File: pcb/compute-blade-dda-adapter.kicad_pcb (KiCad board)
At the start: 2 copper layers, 35.5 x 28.8 mm, 2 parts, among them J1 COMPUTE BLADE, J2 DDA GPS/RTC RIGHT-ANGLE

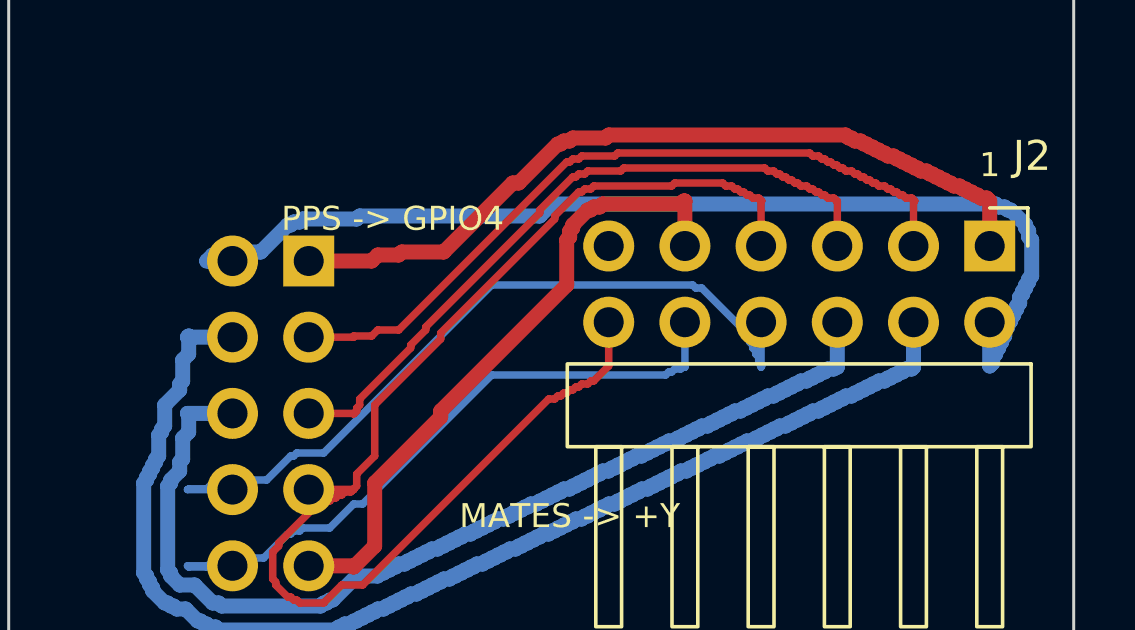
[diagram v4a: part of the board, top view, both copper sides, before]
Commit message: Preserve connector pad escapes during routing
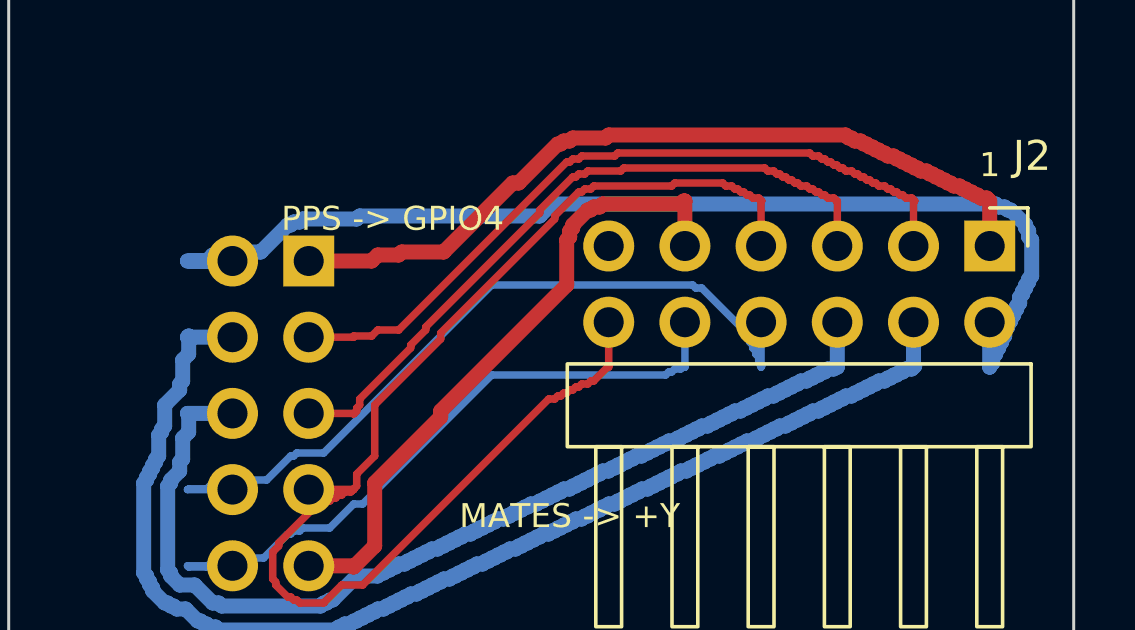
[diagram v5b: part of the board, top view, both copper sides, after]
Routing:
- net 5V_PIN2: track 36.1 -> 37.4 mm
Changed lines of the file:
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@@
   (segment (start 119.8 63.86) (end 119.9 63.76) (width 0.5) (layer "B.Cu") (net 4))
   (segment (start 119.9 63.76) (end 120.1 63.76) (width 0.5) (layer "B.Cu") (net 4))
-  (segment (start 120.1 63.76) (end 120.16 63.7) (width 0.5) (layer "B.Cu") (net 4))
+  (segment (start 120.1 63.76) (end 120.2 63.66) (width 0.5) (layer "B.Cu") (net 4))
+  (segment (start 120.2 63.66) (end 120.16 63.7) (width 0.5) (layer "B.Cu") (net 4))
   (segment (start 120.16 63.7) (end 120.16 62.2) (width 0.5) (layer "B.Cu") (net 4))
-  (segment (start 97.46 60.16) (end 96.6 60.16) (width 0.5) (layer "B.Cu") (net 2))
+  (segment (start 97.46 60.16) (end 95.96 60.16) (width 0.5) (layer "B.Cu") (net 2))
+  (segment (start 95.96 60.16) (end 96.6 60.16) (width 0.5) (layer "B.Cu") (net 2))
   (segment (start 96.6 60.16) (end 96.8 59.96) (width 0.5) (layer "B.Cu") (net 2))
   (segment (start 96.8 59.96) (end 97.5 59.96) (width 0.5) (layer "B.Cu") (net 2))
@@
   (segment (start 122.8 63.36) (end 122.8 63.56) (width 0.5) (layer "B.Cu") (net 2))
   (segment (start 122.8 63.56) (end 122.7 63.66) (width 0.5) (layer "B.Cu") (net 2))
-  (segment (start 122.7 63.66) (end 122.7 62.2) (width 0.5) (layer "B.Cu") (net 2))
-  (segment (start 110 62.2) (end 110 63.66) (width 0.25) (layer "F.Cu") (net 7))
+  (segment (start 122.7 63.66) (end 122.7 63.7) (width 0.5) (layer "B.Cu") (net 2))
+  (segment (start 122.7 63.7) (end 122.7 62.2) (width 0.5) (layer "B.Cu") (net 2))
+  (segment (start 110 62.2) (end 110 63.7) (width 0.25) (layer "F.Cu") (net 7))
+  (segment (start 110 63.7) (end 110 63.66) (width 0.25) (layer "F.Cu") (net 7))
   (segment (start 110 63.66) (end 109.5 64.16) (width 0.25) (layer "F.Cu") (net 7))
   (segment (start 109.5 64.16) (end 109.4 64.16) (width 0.25) (layer "F.Cu") (net 7))

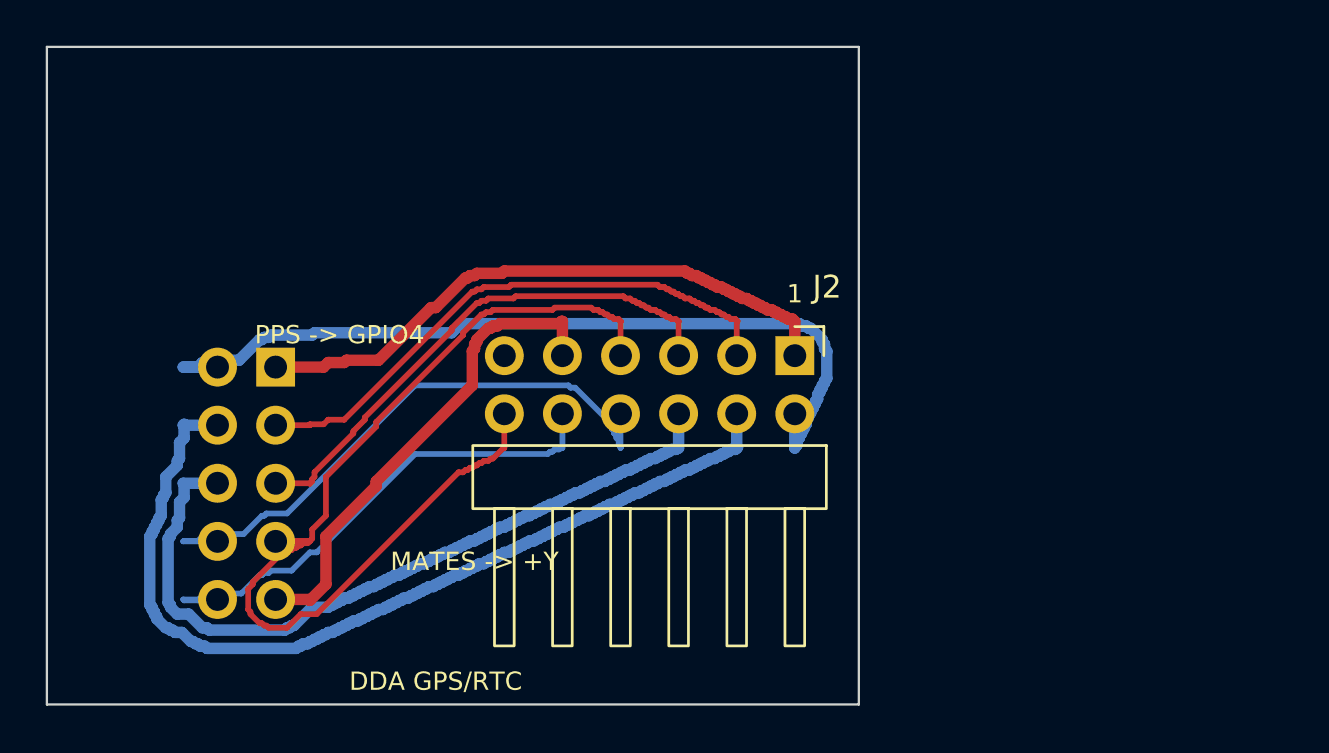
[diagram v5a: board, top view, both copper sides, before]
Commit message: Route 5V pass-through along board perimeter
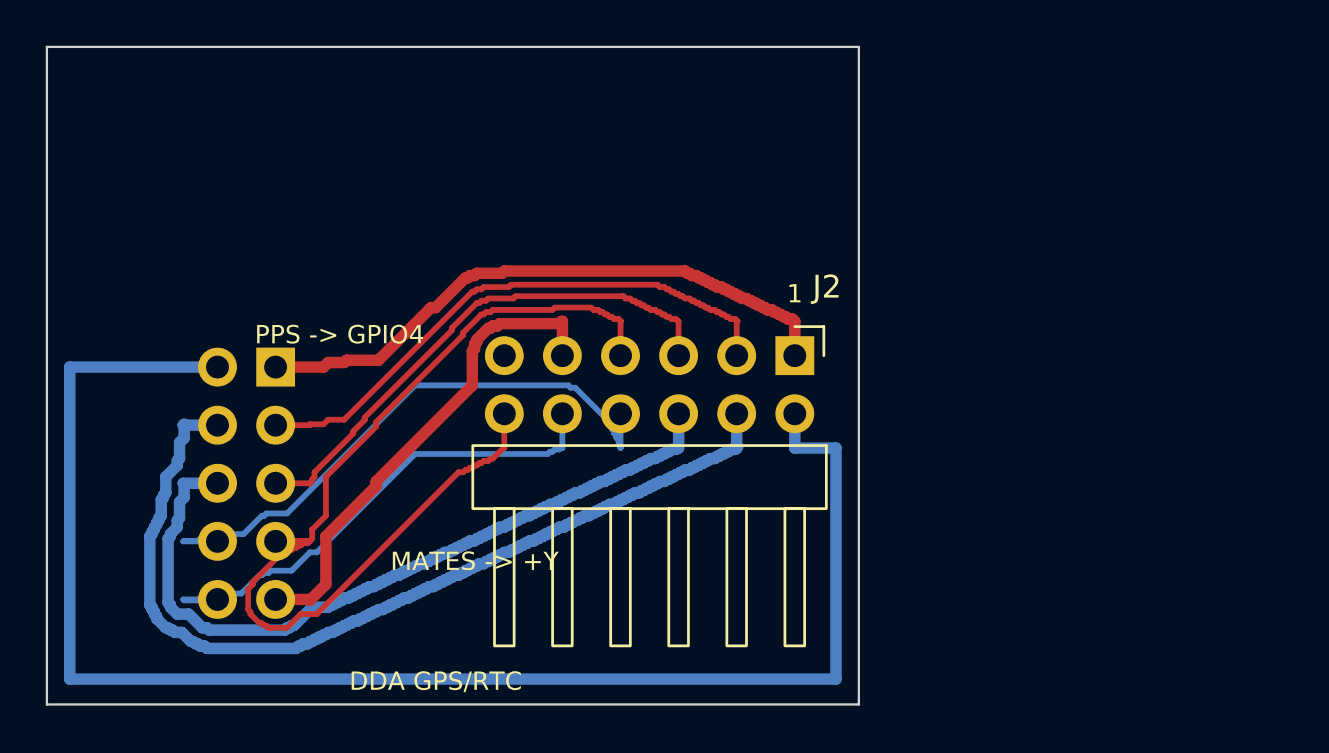
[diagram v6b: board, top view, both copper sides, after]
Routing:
- net 5V_PIN2: track 37.4 -> 67.0 mm
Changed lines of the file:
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@@
   (segment (start 120.2 63.66) (end 120.16 63.7) (width 0.5) (layer "B.Cu") (net 4))
   (segment (start 120.16 63.7) (end 120.16 62.2) (width 0.5) (layer "B.Cu") (net 4))
-  (segment (start 97.46 60.16) (end 95.96 60.16) (width 0.5) (layer "B.Cu") (net 2))
-  (segment (start 95.96 60.16) (end 96.6 60.16) (width 0.5) (layer "B.Cu") (net 2))
-  (segment (start 96.6 60.16) (end 96.8 59.96) (width 0.5) (layer "B.Cu") (net 2))
-  (segment (start 96.8 59.96) (end 97.5 59.96) (width 0.5) (layer "B.Cu") (net 2))
-  (segment (start 97.5 59.96) (end 97.6 59.86) (width 0.5) (layer "B.Cu") (net 2))
-  (segment (start 97.6 59.86) (end 98.4 59.86) (width 0.5) (layer "B.Cu") (net 2))
-  (segment (start 98.4 59.86) (end 99.3 58.96) (width 0.5) (layer "B.Cu") (net 2))
-  (segment (start 99.3 58.96) (end 99.4 58.96) (width 0.5) (layer "B.Cu") (net 2))
-  (segment (start 99.4 58.96) (end 99.5 58.86) (width 0.5) (layer "B.Cu") (net 2))
-  (segment (start 99.5 58.86) (end 99.7 58.86) (width 0.5) (layer "B.Cu") (net 2))
-  (segment (start 99.7 58.86) (end 99.8 58.76) (width 0.5) (layer "B.Cu") (net 2))
-  (segment (start 99.8 58.76) (end 101.6 58.76) (width 0.5) (layer "B.Cu") (net 2))
-  (segment (start 101.6 58.76) (end 101.7 58.66) (width 0.5) (layer "B.Cu") (net 2))
-  (segment (start 101.7 58.66) (end 107.7 58.66) (width 0.5) (layer "B.Cu") (net 2))
-  (segment (start 107.7 58.66) (end 108.1 58.26) (width 0.5) (layer "B.Cu") (net 2))
-  (segment (start 108.1 58.26) (end 122.9 58.26) (width 0.5) (layer "B.Cu") (net 2))
-  (segment (start 122.9 58.26) (end 123 58.36) (width 0.5) (layer "B.Cu") (net 2))
-  (segment (start 123 58.36) (end 123.2 58.36) (width 0.5) (layer "B.Cu") (net 2))
-  (segment (start 123.2 58.36) (end 123.3 58.46) (width 0.5) (layer "B.Cu") (net 2))
-  (segment (start 123.3 58.46) (end 123.4 58.46) (width 0.5) (layer "B.Cu") (net 2))
-  (segment (start 123.4 58.46) (end 123.9 58.96) (width 0.5) (layer "B.Cu") (net 2))
-  (segment (start 123.9 58.96) (end 123.9 59.06) (width 0.5) (layer "B.Cu") (net 2))
-  (segment (start 123.9 59.06) (end 124 59.16) (width 0.5) (layer "B.Cu") (net 2))
-  (segment (start 124 59.16) (end 124 59.36) (width 0.5) (layer "B.Cu") (net 2))
-  (segment (start 124 59.36) (end 124.1 59.46) (width 0.5) (layer "B.Cu") (net 2))
-  (segment (start 124.1 59.46) (end 124.1 60.66) (width 0.5) (layer "B.Cu") (net 2))
-  (segment (start 124.1 60.66) (end 124 60.76) (width 0.5) (layer "B.Cu") (net 2))
-  (segment (start 124 60.76) (end 124 60.86) (width 0.5) (layer "B.Cu") (net 2))
-  (segment (start 124 60.86) (end 123.9 60.96) (width 0.5) (layer "B.Cu") (net 2))
-  (segment (start 123.9 60.96) (end 123.9 61.06) (width 0.5) (layer "B.Cu") (net 2))
-  (segment (start 123.9 61.06) (end 123.8 61.16) (width 0.5) (layer "B.Cu") (net 2))
-  (segment (start 123.8 61.16) (end 123.8 61.26) (width 0.5) (layer "B.Cu") (net 2))
-  (segment (start 123.8 61.26) (end 123.7 61.36) (width 0.5) (layer "B.Cu") (net 2))
-  (segment (start 123.7 61.36) (end 123.7 61.56) (width 0.5) (layer "B.Cu") (net 2))
-  (segment (start 123.7 61.56) (end 123.6 61.66) (width 0.5) (layer "B.Cu") (net 2))
-  (segment (start 123.6 61.66) (end 123.6 61.76) (width 0.5) (layer "B.Cu") (net 2))
-  (segment (start 123.6 61.76) (end 123.5 61.86) (width 0.5) (layer "B.Cu") (net 2))
-  (segment (start 123.5 61.86) (end 123.5 61.96) (width 0.5) (layer "B.Cu") (net 2))
-  (segment (start 123.5 61.96) (end 123.4 62.06) (width 0.5) (layer "B.Cu") (net 2))
-  (segment (start 123.4 62.06) (end 123.4 62.16) (width 0.5) (layer "B.Cu") (net 2))
-  (segment (start 123.4 62.16) (end 123.3 62.26) (width 0.5) (layer "B.Cu") (net 2))
-  (segment (start 123.3 62.26) (end 123.3 62.36) (width 0.5) (layer "B.Cu") (net 2))
-  (segment (start 123.3 62.36) (end 123.2 62.46) (width 0.5) (layer "B.Cu") (net 2))
-  (segment (start 123.2 62.46) (end 123.2 62.66) (width 0.5) (layer "B.Cu") (net 2))
-  (segment (start 123.2 62.66) (end 123.1 62.76) (width 0.5) (layer "B.Cu") (net 2))
-  (segment (start 123.1 62.76) (end 123.1 62.86) (width 0.5) (layer "B.Cu") (net 2))
-  (segment (start 123.1 62.86) (end 123 62.96) (width 0.5) (layer "B.Cu") (net 2))
-  (segment (start 123 62.96) (end 123 63.06) (width 0.5) (layer "B.Cu") (net 2))
-  (segment (start 123 63.06) (end 122.9 63.16) (width 0.5) (layer "B.Cu") (net 2))
-  (segment (start 122.9 63.16) (end 122.9 63.26) (width 0.5) (layer "B.Cu") (net 2))
-  (segment (start 122.9 63.26) (end 122.8 63.36) (width 0.5) (layer "B.Cu") (net 2))
-  (segment (start 122.8 63.36) (end 122.8 63.56) (width 0.5) (layer "B.Cu") (net 2))
-  (segment (start 122.8 63.56) (end 122.7 63.66) (width 0.5) (layer "B.Cu") (net 2))
-  (segment (start 122.7 63.66) (end 122.7 63.7) (width 0.5) (layer "B.Cu") (net 2))
+  (segment (start 97.46 60.16) (end 91 60.16) (width 0.5) (layer "B.Cu") (net 2))
+  (segment (start 91 60.16) (end 91 73.8) (width 0.5) (layer "B.Cu") (net 2))
+  (segment (start 91 73.8) (end 124.5 73.8) (width 0.5) (layer "B.Cu") (net 2))
+  (segment (start 124.5 73.8) (end 124.5 63.7) (width 0.5) (layer "B.Cu") (net 2))
+  (segment (start 124.5 63.7) (end 122.7 63.7) (width 0.5) (layer "B.Cu") (net 2))
   (segment (start 122.7 63.7) (end 122.7 62.2) (width 0.5) (layer "B.Cu") (net 2))
   (segment (start 110 62.2) (end 110 63.7) (width 0.25) (layer "F.Cu") (net 7))

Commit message: Redesign adapter for parallel DDA stack
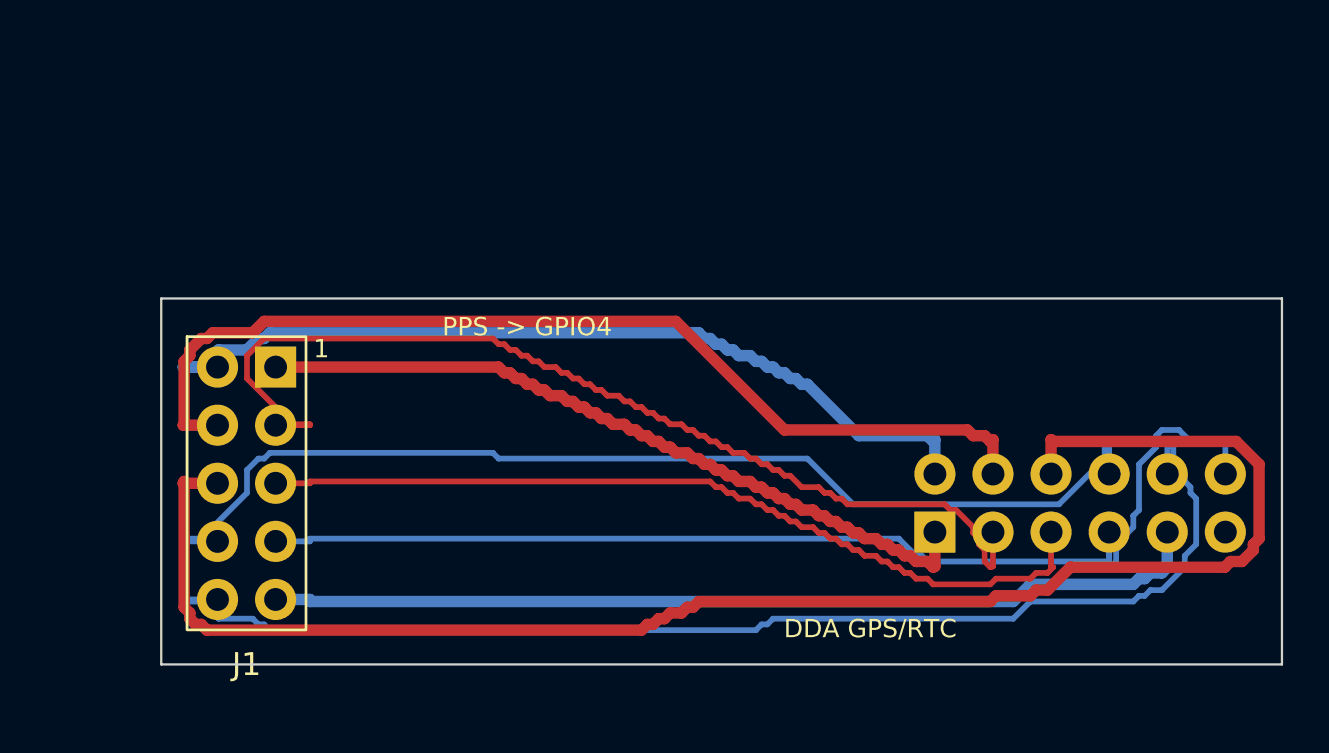
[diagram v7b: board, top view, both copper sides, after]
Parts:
- J1: value COMPUTE BLADE -> HLE-105-02-L-DV-PE-BE; footprint Connector_PinSocket_2.54mm:PinSocket_2x05_P2.54mm_Vertical -> Adapter:Samtec_HLE-105-02-L-DV-PE-BE; moved to F.Cu
- J2: value DDA GPS/RTC RIGHT-ANGLE -> MTLW-106-06-G-D-035 REVERSE; footprint Connector_PinHeader_2.54mm:PinHeader_2x06_P2.54mm_Horizontal -> Adapter:Samtec_MTLW-106-06-G-D-035_Reverse; moved to B.Cu
- moved J2 9.85 mm to (128.8, 67.4), turned to 90 degrees
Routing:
- net GND_PIN6: track 34.7 -> 70.7 mm
- net UART_RX_FROM_GPS_TX: track 22.4 -> 54.8 mm
- net 5V_PIN2: track 67.0 -> 38.5 mm
- net UART_TX_TO_GPS_RX: track 26.5 -> 48.2 mm
- net SDA_GPIO2: track 25.0 -> 45.3 mm
- net GND_PIN9: track 21.5 -> 41.2 mm
- net SCL_GPIO3: track 23.3 -> 37.9 mm
- net 3V3: track 26.9 -> 34.0 mm
- net PPS_GPIO4: track 45.0 -> 51.7 mm
- net 5V_PIN4: track 41.9 -> 44.2 mm
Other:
- board size 35.5 x 28.8 mm -> 49 x 16 mm
